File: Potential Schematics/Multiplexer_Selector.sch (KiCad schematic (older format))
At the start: 15 parts

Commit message: Finished PCB
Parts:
- removed U? (x8): 74LS08, symbol 74xx:74LS08
- added U28, U290, U291: 74LS08, Daniel_Kopp:DIP-14_300_ELL, symbol 4-bit_processor-rescue:74LS08
- U269, U281, U292: renamed from U?; footprint (none) -> Daniel_Kopp:DIP-14_300_ELL
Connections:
- wire segments 88 -> 92

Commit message: Made Multiplier
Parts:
- removed U269: 74LS04, Daniel_Kopp:DIP-14_300_ELL, symbol 4-bit_processor-rescue:74LS04
- removed U28, U290, U291: 74LS08, Daniel_Kopp:DIP-14_300_ELL, symbol 4-bit_processor-rescue:74LS08
- removed U281, U292: 74LS32, Daniel_Kopp:DIP-14_300_ELL, symbol 4-bit_processor-rescue:74LS32
- added U? (x3): 74LS04, symbol 4-bit_processor-rescue:74LS04
- added U? (x8): 74LS32, symbol 4-bit_processor-rescue:74LS32
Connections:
- net GND: now also U?.7 (GND), U?.7 (GND), U?.7 (GND), U?.7 (GND), U?.7 (GND), U?.7 (GND), U?.7 (GND), U?.7 (GND), U?.7 (GND), U?.7 (GND), U?.7 (GND)
- net Q0: now also U?.3
- net Q1: now also U?.3
- net Q2: now also U?.3
- net Q3: now also U?.3
- net S0: now also U?.1
- net S1: now also U?.1
- net S3: now also U?.1
- net VCC: now also U?.14 (VCC), U?.14 (VCC), U?.14 (VCC), U?.14 (VCC), U?.14 (VCC), U?.14 (VCC), U?.14 (VCC), U?.14 (VCC), U?.14 (VCC), U?.14 (VCC), U?.14 (VCC)
- new net: U?.1, U?.3 (x4)
- new net On_Off/Q0: U?.1
- new net On_Off/Q1: U?.1
- new net On_Off/Q2: U?.1
- new net On_Off/Q3: U?.1
- new net On_Off/S3: U?.2
- new net sheet5BB302C7/Q0: U?.2
- new net sheet5BB302C7/Q1: U?.2
- new net sheet5BB302C7/Q2: U?.2
- new net sheet5BB302C7/Q3: U?.2
- new net sheet5BB302C7/S0: U?.2
- new net sheet5BB303AD/Q0: U?.2
- new net sheet5BB303AD/Q1: U?.2
- new net sheet5BB303AD/Q2: U?.2
- new net sheet5BB303AD/Q3: U?.2
- new net sheet5BB303AD/S1: U?.2

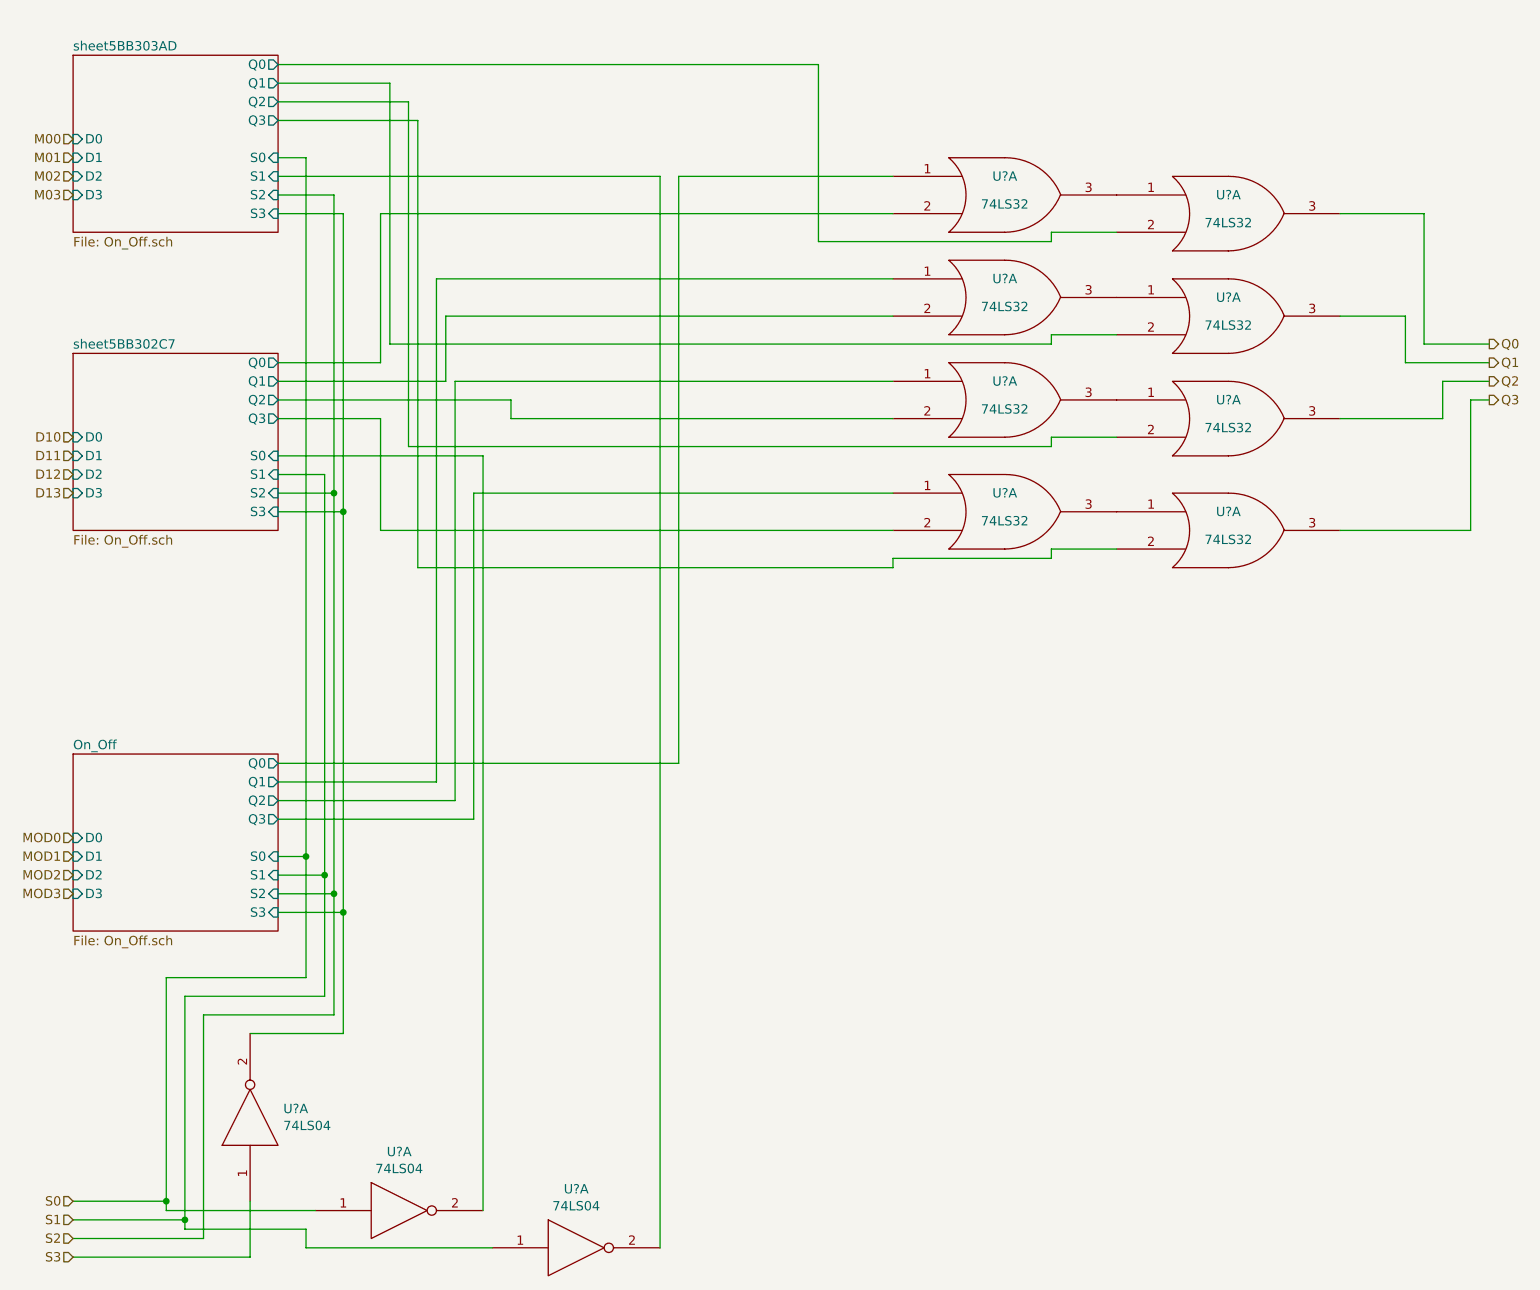
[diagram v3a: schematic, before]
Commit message: Updated overview of Schematic
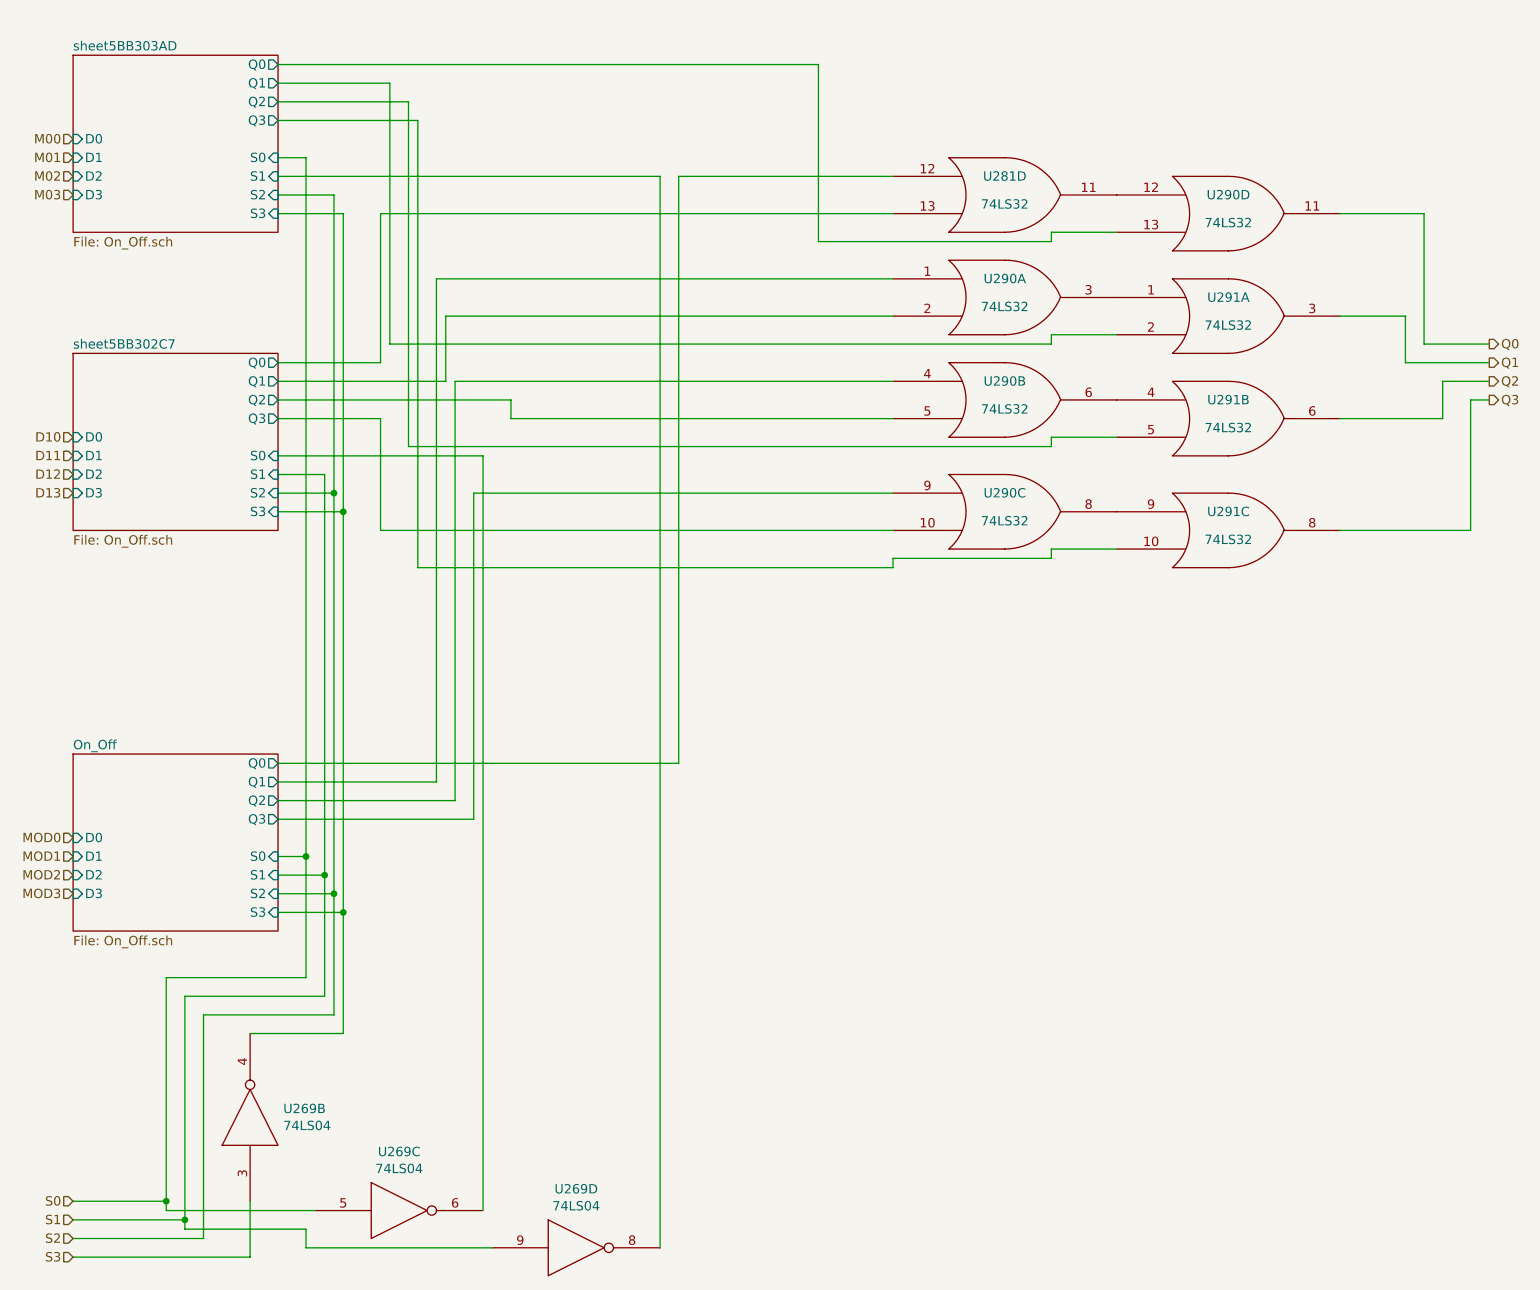
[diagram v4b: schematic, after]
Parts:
- gave numbers to parts that had none: 4
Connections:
- net On_Off/Q0: now also U281.12; no longer U281.1
- net On_Off/Q2: now also U290.4; no longer U290.1
- net On_Off/Q3: now also U290.9; no longer U290.1
- net On_Off/S3: now also U269.4; no longer U269.2
- net Q0: now also U290.11; no longer U290.3
- net Q2: now also U291.6; no longer U291.3
- net Q3: now also U291.8; no longer U291.3
- net S0: now also U269.5; no longer U269.1
- net S1: now also U269.9; no longer U269.1
- net S3: now also U269.3; no longer U269.1
- net sheet5BB302C7/Q0: now also U281.13; no longer U281.2
- net sheet5BB302C7/Q2: now also U290.5; no longer U290.2
- net sheet5BB302C7/Q3: now also U290.10; no longer U290.2
- net sheet5BB302C7/S0: now also U269.6; no longer U269.2
- net sheet5BB303AD/Q0: now also U290.13; no longer U290.2
- net sheet5BB303AD/Q2: now also U291.5; no longer U291.2
- net sheet5BB303AD/Q3: now also U291.10; no longer U291.2
- net sheet5BB303AD/S1: now also U269.8; no longer U269.2
- new net: U281.11, U290.12
- new net: U290.6, U291.4
- new net: U290.8, U291.9
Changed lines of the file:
@@
 $Descr A4 11693 8268
 encoding utf-8
-Sheet 451 467
+Sheet 451 902
 Title ""
 Date ""
@@
 $EndSheet
 $Comp
-L 4-bit_processor-rescue:74LS04 U?
-U 1 1 5BB34644
+L 4-bit_processor-rescue:74LS04 U269
+U 2 1 5BB34644
 P 2800 6950
-F 0 "U?" V 2846 6772 50  0000 R CNN
+F 0 "U269" V 2846 6772 50  0000 R CNN
 F 1 "74LS04" V 2755 6772 50  0000 R CNN
 F 2 "" H 2800 6950 50  0001 C CNN
 F 3 "" H 2800 6950 50  0001 C CNN
-	1    2800 6950
+	2    2800 6950
 	0    -1   -1   0
 $EndComp
@@
 	1850 7400 2350 7400
 $Comp
-L 4-bit_processor-rescue:74LS04 U?
-U 1 1 5BB37254
+L 4-bit_processor-rescue:74LS04 U269
+U 3 1 5BB37254
 P 3600 7450
-F 0 "U?" H 3600 7765 50  0000 C CNN
+F 0 "U269" H 3600 7765 50  0000 C CNN
 F 1 "74LS04" H 3600 7674 50  0000 C CNN
 F 2 "" H 3600 7450 50  0001 C CNN
 F 3 "" H 3600 7450 50  0001 C CNN
-	1    3600 7450
-	1    0    0    -1
-$EndComp
-$Comp
-L 4-bit_processor-rescue:74LS04 U?
-U 1 1 5BB37D71
+	3    3600 7450
+	1    0    0    -1
+$EndComp
+$Comp
+L 4-bit_processor-rescue:74LS04 U269
+U 4 1 5BB37D71
 P 4550 7650
-F 0 "U?" H 4550 7965 50  0000 C CNN
+F 0 "U269" H 4550 7965 50  0000 C CNN
 F 1 "74LS04" H 4550 7874 50  0000 C CNN
 F 2 "" H 4550 7650 50  0001 C CNN
 F 3 "" H 4550 7650 50  0001 C CNN
-	1    4550 7650
+	4    4550 7650
 	1    0    0    -1
 $EndComp
@@
 	5000 1900 5000 7650
 $Comp
-L 4-bit_processor-rescue:74LS32 U?
-U 1 1 5BB3E441
+L 4-bit_processor-rescue:74LS32 U281
+U 4 1 5BB3E441
 P 6850 2000
-F 0 "U?" H 6850 2100 50  0000 C CNN
+F 0 "U281" H 6850 2100 50  0000 C CNN
 F 1 "74LS32" H 6850 1950 50  0000 C CNN
 F 2 "" H 6850 2000 50  0001 C CNN
 F 3 "" H 6850 2000 50  0001 C CNN
-	1    6850 2000
-	1    0    0    -1
-$EndComp
-$Comp
-L 4-bit_processor-rescue:74LS32 U?
-U 1 1 5BB44214
+	4    6850 2000
+	1    0    0    -1
+$EndComp
+$Comp
+L 4-bit_processor-rescue:74LS32 U290
+U 4 1 5BB44214
 P 8050 2100
-F 0 "U?" H 8050 2200 50  0000 C CNN
+F 0 "U290" H 8050 2200 50  0000 C CNN
 F 1 "74LS32" H 8050 2050 50  0000 C CNN
 F 2 "" H 8050 2100 50  0001 C CNN
 F 3 "" H 8050 2100 50  0001 C CNN
-	1    8050 2100
+	4    8050 2100
 	1    0    0    -1
 $EndComp
@@
 	7100 2200 7100 2250
 $Comp
-L 4-bit_processor-rescue:74LS32 U?
+L 4-bit_processor-rescue:74LS32 U290
 U 1 1 5BB45336
 P 6850 2550
-F 0 "U?" H 6850 2650 50  0000 C CNN
+F 0 "U290" H 6850 2650 50  0000 C CNN
 F 1 "74LS32" H 6850 2500 50  0000 C CNN
 F 2 "" H 6850 2550 50  0001 C CNN
@@
 $EndComp
 $Comp
-L 4-bit_processor-rescue:74LS32 U?
+L 4-bit_processor-rescue:74LS32 U291
 U 1 1 5BB4533D
 P 8050 2650
-F 0 "U?" H 8050 2750 50  0000 C CNN
+F 0 "U291" H 8050 2750 50  0000 C CNN
 F 1 "74LS32" H 8050 2600 50  0000 C CNN
 F 2 "" H 8050 2650 50  0001 C CNN
@@
 	7100 2750 7100 2800
 $Comp
-L 4-bit_processor-rescue:74LS32 U?
-U 1 1 5BB45D4A
+L 4-bit_processor-rescue:74LS32 U290
+U 2 1 5BB45D4A
 P 6850 3100
-F 0 "U?" H 6850 3200 50  0000 C CNN
+F 0 "U290" H 6850 3200 50  0000 C CNN
 F 1 "74LS32" H 6850 3050 50  0000 C CNN
 F 2 "" H 6850 3100 50  0001 C CNN
 F 3 "" H 6850 3100 50  0001 C CNN
-	1    6850 3100
-	1    0    0    -1
-$EndComp
-$Comp
-L 4-bit_processor-rescue:74LS32 U?
-U 1 1 5BB45D51
+	2    6850 3100
+	1    0    0    -1
+$EndComp
+$Comp
+L 4-bit_processor-rescue:74LS32 U291
+U 2 1 5BB45D51
 P 8050 3200
-F 0 "U?" H 8050 3300 50  0000 C CNN
+F 0 "U291" H 8050 3300 50  0000 C CNN
 F 1 "74LS32" H 8050 3150 50  0000 C CNN
 F 2 "" H 8050 3200 50  0001 C CNN
 F 3 "" H 8050 3200 50  0001 C CNN
-	1    8050 3200
+	2    8050 3200
 	1    0    0    -1
 $EndComp
@@
 	7100 3300 7100 3350
 $Comp
-L 4-bit_processor-rescue:74LS32 U?
-U 1 1 5BB46801
+L 4-bit_processor-rescue:74LS32 U290
+U 3 1 5BB46801
 P 6850 3700
-F 0 "U?" H 6850 3800 50  0000 C CNN
+F 0 "U290" H 6850 3800 50  0000 C CNN
 F 1 "74LS32" H 6850 3650 50  0000 C CNN
 F 2 "" H 6850 3700 50  0001 C CNN
 F 3 "" H 6850 3700 50  0001 C CNN
-	1    6850 3700
-	1    0    0    -1
-$EndComp
-$Comp
-L 4-bit_processor-rescue:74LS32 U?
-U 1 1 5BB46808
+	3    6850 3700
+	1    0    0    -1
+$EndComp
+$Comp
+L 4-bit_processor-rescue:74LS32 U291
+U 3 1 5BB46808
 P 8050 3800
-F 0 "U?" H 8050 3900 50  0000 C CNN
+F 0 "U291" H 8050 3900 50  0000 C CNN
 F 1 "74LS32" H 8050 3750 50  0000 C CNN
 F 2 "" H 8050 3800 50  0001 C CNN
 F 3 "" H 8050 3800 50  0001 C CNN
-	1    8050 3800
-	1    0    0    -1
-$EndComp
+	3    8050 3800
+	1    0    0    -1
+$EndComp
